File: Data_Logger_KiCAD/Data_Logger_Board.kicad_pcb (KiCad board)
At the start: 4 copper layers, 45 x 64.8 mm, 110 parts, among them J1 USB_C_Receptacle_USB2.0_16P, J2 Screw_Terminal_01x02, J3 Micro_SD_Card, J4 Conn_Coaxial_Small, J5 Conn_01x02, Q1 Q_NMOS_GSD, SW1 SW_Push, SW2 SW_Push, U1 LSM6DSO32TR, U10 BMP390L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

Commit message: fix merge
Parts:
- moved C37 8.78 mm to (158.2, 96.6), turned to 180 degrees
- moved D5 3.10 mm to (162.1, 96.6)
- moved R25 2.10 mm to (121.4, 55.7)
- moved R20 0.90 mm to (156.7, 106.4)
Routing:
- net +3V3: track 166.9 -> 85.8 mm, vias 27 -> 25
- net Net-(U6-VBAT): track 19.4 -> 13.0 mm, vias 3 -> 2
- net Net-(D6-A): track 2.12 -> 0.00 mm
- net /MCU/~{MS_CS}: track 45.4 -> 43.9 mm
- net +BATT: track 2.79 -> 4.22 mm
- net /MCU/PWR_IN: track 23.4 -> 24.5 mm
- net Net-(D2-A): track 2.10 -> 1.20 mm
- net /MCU/MOSI: track 113.3 -> 112.4 mm
- net /MCU/RADIO_INT: track 19.8 -> 19.0 mm
- net /MCU/BATTERY_SENSE: track 23.2 -> 23.9 mm
- net /MCU/ANT_SW: track 48.0 -> 47.5 mm
- net /MCU/~{IMU_CS}: track 29.4 -> 29.5 mm, vias 2 -> 3
- net GND: vias 457 -> 510
- added copper zone on In3.Cu, net +3V3
- added copper zone on In4.Cu, net GND
- removed copper zone on In2.Cu, net +3V3
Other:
- copper layers 4 -> 6

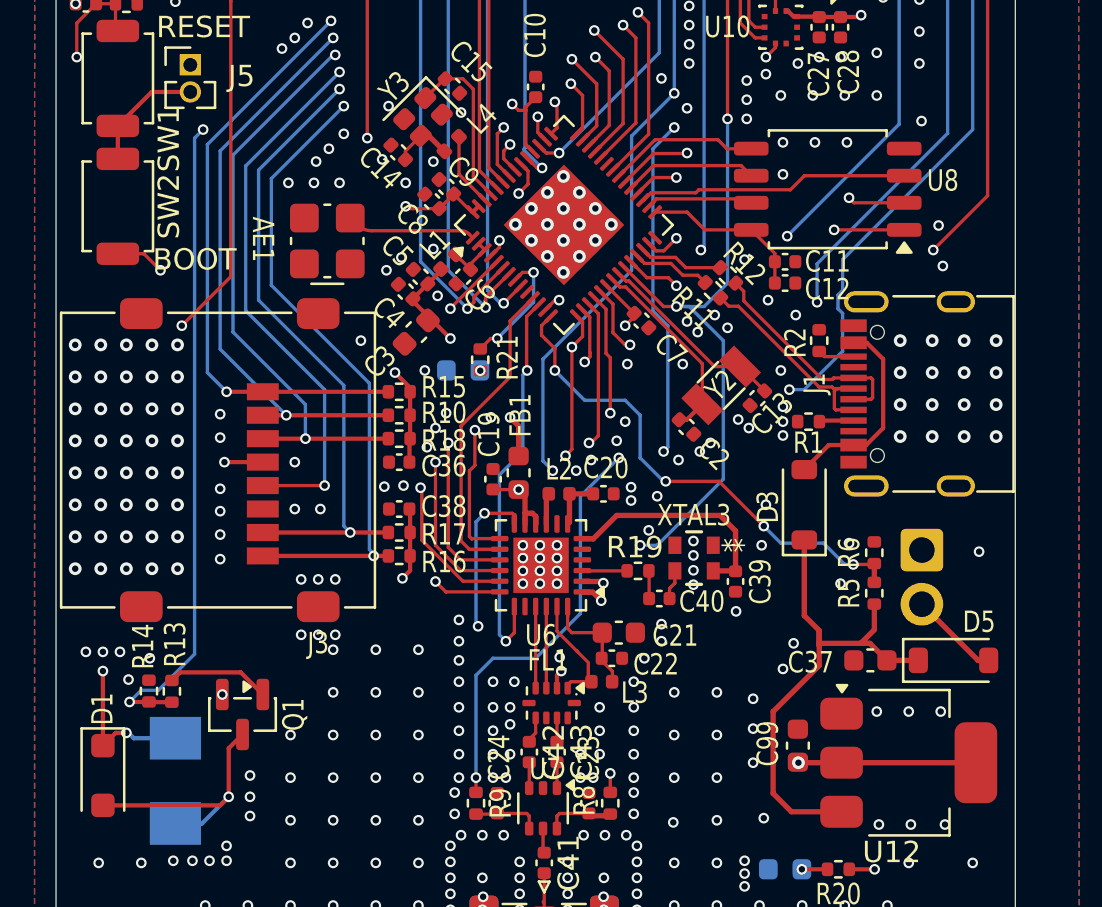
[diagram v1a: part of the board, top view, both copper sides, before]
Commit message: four layer creation
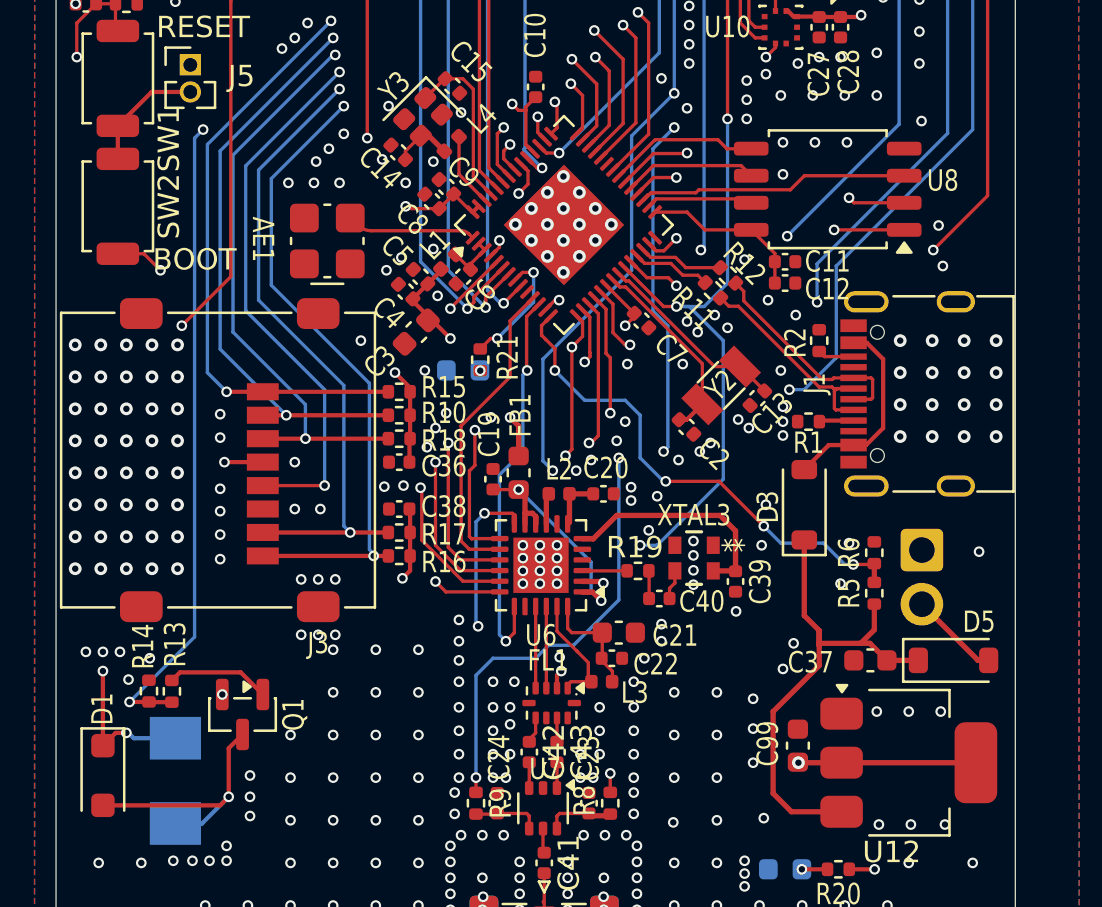
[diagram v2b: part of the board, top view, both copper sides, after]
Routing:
- net Net-(U6-VBAT): track 13.0 -> 12.3 mm
- net /MCU/ANT_SW: track 47.5 -> 48.2 mm
- removed copper zone on In3.Cu, net +3V3
- removed copper zone on In4.Cu, net GND
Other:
- copper layers 6 -> 4
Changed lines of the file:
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@@
 		(4 "In1.Cu" power)
 		(6 "In2.Cu" signal)
-		(8 "In3.Cu" signal)
-		(10 "In4.Cu" power)
 		(2 "B.Cu" signal)
 		(9 "F.Adhes" user "F.Adhesive")
@@
 			(layer "dielectric 1"
 				(type "prepreg")
-				(thickness 0.0994)
+				(thickness 0.1)
 				(material "3313*1")
 				(epsilon_r 4.5)
@@
 			(layer "dielectric 2"
 				(type "core")
-				(thickness 0.55)
+				(thickness 1.238)
 				(material "Core")
 				(epsilon_r 4.5)
@@
 			(layer "dielectric 3"
 				(type "prepreg")
-				(thickness 0.1088)
+				(thickness 0.1)
 				(material "2116*1")
 				(epsilon_r 4.5)
 				(loss_tangent 0.02)
 			)
-			(layer "In3.Cu"
-				(type "copper")
-				(thickness 0.0152)
-			)
-			(layer "dielectric 4"
-				(type "core")
-				(thickness 0.55)
-				(material "Core")
-				(epsilon_r 4.5)
-				(loss_tangent 0.02)
-			)
-			(layer "In4.Cu"
-				(type "copper")
-				(thickness 0.0152)
-			)
-			(layer "dielectric 5"
-				(type "prepreg")
-				(thickness 0.0994)
-				(material "3313*1")
-				(epsilon_r 4.5)
-				(loss_tangent 0.02)
-			)
 			(layer "B.Cu"
 				(type "copper")
@@
 			(net 0)
 			(net_name "")
-			(layers "F.Cu" "B.Cu" "In1.Cu" "In2.Cu" "In3.Cu" "In4.Cu")
+			(layers "F.Cu" "B.Cu" "In1.Cu" "In2.Cu")
 			(hatch edge 0.508)
 			(connect_pads
@@
 			(net 0)
 			(net_name "")
-			(layers "F.Cu" "B.Cu" "In1.Cu" "In2.Cu" "In3.Cu" "In4.Cu")
+			(layers "F.Cu" "B.Cu" "In1.Cu" "In2.Cu")
 			(hatch edge 0.508)
 			(connect_pads
@@
 			(net 0)
 			(net_name "")
-			(layers "B.Cu" "In1.Cu" "F.SilkS" "In2.Cu" "In3.Cu" "In4.Cu")
+			(layers "B.Cu" "In1.Cu" "F.SilkS" "In2.Cu")
 			(hatch edge 0.508)
 			(connect_pads
@@
 	)
 	(segment
-		(start 142.5 96.5)
-		(end 144.6 94.4)
+		(start 140.5 96.5)
+		(end 139.7 97.3)
 		(width 0.1565)
 		(layer "B.Cu")
@@
 	)
 	(segment
-		(start 148 80.2)
-		(end 148.7 80.9)
+		(start 146.4 93.765899)
+		(end 144.275149 95.89075)
 		(width 0.1565)
 		(layer "B.Cu")
@@
 	)
 	(segment
-		(start 140.5 96.5)
-		(end 142.5 96.5)
+		(start 139.7 97.3)
+		(end 139.7 102.1)
+		(width 0.1565)
+		(layer "B.Cu")
+		(net 37)
+	)
+	(segment
+		(start 148 80.2)
+		(end 148.7 80.9)
 		(width 0.1565)
 		(layer "B.Cu")
@@
 	)
 	(segment
+		(start 143.10925 95.89075)
+		(end 142.5 96.5)
+		(width 0.1565)
+		(layer "B.Cu")
+		(net 37)
+	)
+	(segment
 		(start 148 72.6)
 		(end 148 80.2)
@@
 	)
 	(segment
-		(start 144.6 94.4)
-		(end 144.6 88.9)
+		(start 146.4 87.1)
+		(end 146.4 93.765899)
 		(width 0.1565)
 		(layer "B.Cu")
@@
 	)
 	(segment
-		(start 139.7 97.3)
-		(end 140.5 96.5)
+		(start 144.275149 95.89075)
+		(end 143.10925 95.89075)
 		(width 0.1565)
 		(layer "B.Cu")
@@
 	)
 	(segment
-		(start 139.7 102.1)
-		(end 139.7 97.3)
+		(start 142.5 96.5)
+		(end 140.5 96.5)
 		(width 0.1565)
 		(layer "B.Cu")
@@
 	)
 	(segment
-		(start 144.6 88.9)
-		(end 146.4 87.1)
-		(width 0.1565)
-		(layer "B.Cu")
-		(net 37)
-	)
-	(segment
 		(start 148.5 86.8)
 		(end 146.7 86.8)
@@
 	)
 	(segment
-		(start 126.9 71.7)
-		(end 126.5 72.1)
-		(width 0.1565)
-		(layer "B.Cu")
-		(net 40)
-	)
-	(segment
 		(start 126.5 72.1)
-		(end 126.5 96.3)
-		(width 0.1565)
-		(layer "B.Cu")
-		(net 40)
-	)
-	(segment
-		(start 124.8 98)
-		(end 124 98)
+		(end 126.5 95.5)
 		(width 0.1565)
 		(layer "B.Cu")
@@
 	)
 	(segment
-		(start 126.5 96.3)
-		(end 124.8 98)
+		(start 126.5 95.5)
+		(end 123.45 98.55)
 		(width 0.1565)
 		(layer "B.Cu")
@@
 	)
 	(segment
-		(start 124 98)
-		(end 123.45 98.55)
+		(start 126.9 71.7)
+		(end 126.5 72.1)
 		(width 0.1565)
 		(layer "B.Cu")
@@
 	)
 	(segment
-		(start 156.9 77.8)
-		(end 163 71.7)
-		(width 0.1565)
-		(layer "B.Cu")
-		(net 64)
-	)
-	(segment
-		(start 154.4 83.9)
-		(end 155.1 83.9)
-		(width 0.1565)
-		(layer "B.Cu")
-		(net 64)
-	)
-	(segment
-		(start 156.9 80.322026)
-		(end 156.68075 80.102776)
-		(width 0.1565)
-		(layer "B.Cu")
-		(net 64)
-	)
-	(segment
-		(start 156.9 82.1)
-		(end 156.9 80.322026)
-		(width 0.1565)
-		(layer "B.Cu")
-		(net 64)
-	)
-	(segment
-		(start 156.68075 80.102776)
-		(end 156.68075 79.457224)
+		(start 155.1 83.9)
+		(end 156.6 82.4)
 		(width 0.1565)
 		(layer "B.Cu")
@@
 	)
 	(segment
-		(start 156.9 79.237974)
-		(end 156.9 77.8)
+		(start 163 71.7)
+		(end 163 60.225)
 		(width 0.1565)
 		(layer "B.Cu")
@@
 	)
 	(segment
-		(start 155.1 83.9)
-		(end 156.9 82.1)
+		(start 154.4 83.9)
+		(end 155.1 83.9)
 		(width 0.1565)
 		(layer "B.Cu")
@@
 	)
 	(segment
-		(start 163 71.7)
-		(end 163 60.225)
+		(start 163 60.225)
+		(end 162.475 59.7)
 		(width 0.1565)
 		(layer "B.Cu")
@@
 	)
 	(segment
-		(start 156.68075 79.457224)
-		(end 156.9 79.237974)
+		(start 156.6 82.4)
+		(end 156.6 78.1)
 		(width 0.1565)
 		(layer "B.Cu")
@@
 	)
 	(segment
-		(start 163 60.225)
-		(end 162.475 59.7)
+		(start 156.6 78.1)
+		(end 163 71.7)
 		(width 0.1565)
 		(layer "B.Cu")
@@
 	)
 	(segment
-		(start 145.11575 93.34075)
-		(end 145.575 93.8)
+		(start 145.1 93.325)
+		(end 145.1 91.9875)
 		(width 0.1565)
-		(layer "In3.Cu")
-		(net 112)
-	)
-	(segment
-		(start 144.5 90.1)
-		(end 145.11575 90.71575)
-		(width 0.1565)
-		(layer "In3.Cu")
-		(net 112)
-	)
-	(segment
-		(start 141.7 88.5875)
-		(end 143.2125 90.1)
-		(width 0.1565)
-		(layer "In3.Cu")
+		(layer "B.Cu")
 		(net 112)
 	)
 	(segment
-		(start 143.2125 90.1)
-		(end 144.5 90.1)
+		(start 145.1 91.9875)
+		(end 141.7 88.5875)
 		(width 0.1565)
-		(layer "In3.Cu")
+		(layer "B.Cu")
 		(net 112)
 	)
 	(segment
-		(start 145.11575 90.71575)
-		(end 145.11575 93.34075)
+		(start 145.575 93.8)
+		(end 145.1 93.325)
 		(width 0.1565)
-		(layer "In3.Cu")
+		(layer "B.Cu")
 		(net 112)
 	)
@@
 		(net 1)
 		(net_name "GND")
-		(layers "F.Cu" "B.Cu" "In1.Cu" "In2.Cu" "In4.Cu")
+		(layers "F.Cu" "B.Cu" "In1.Cu" "In2.Cu")
 		(hatch edge 0.5)
 		(connect_pads yes
@@
 			)
 		)
-	)
-	(zone
-		(net 5)
-		(net_name "+3V3")
-		(layer "In3.Cu")
-		(hatch edge 0.5)
-		(priority 3)
-		(connect_pads yes
-			(clearance 0.127)
-		)
-		(min_thickness 0.127)
-		(filled_areas_thickness no)
-		(fill yes
-			(thermal_gap 0.5)
-			(thermal_bridge_width 0.5)
-		)
-		(polygon
-			(pts
-				(xy 119 34.5) (xy 167.95 34.4) (xy 168 115.15) (xy 119 115.2)
-			)
-		)

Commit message: start power routing
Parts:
- moved R25 2.10 mm to (121.3, 57.8)
- moved R20 0.90 mm to (157.6, 106.4)
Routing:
- net +3V3: track 85.8 -> 185.9 mm, vias 25 -> 26
- net /MCU/ACCEL_INT: track 52.1 -> 54.3 mm
- net Net-(D6-A): track 0.00 -> 2.12 mm
- net Net-(D2-A): track 1.20 -> 2.10 mm
- net /MCU/~{IMU_CS}: track 29.5 -> 29.4 mm, vias 3 -> 2
- net GND: vias 510 -> 473
- added copper zone on In2.Cu, net +3V3

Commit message: ready for review
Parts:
- moved C37 8.78 mm to (154.8, 104.7), turned to -90 degrees
- moved D5 3.10 mm to (159.0, 96.6)
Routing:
- net +3V3: track 185.9 -> 159.8 mm, vias 26 -> 27
- net Net-(U6-VBAT): track 12.3 -> 19.4 mm, vias 2 -> 3
- net /MCU/ACCEL_INT: track 54.3 -> 52.1 mm
- net +BATT: track 4.22 -> 2.79 mm
- net /MCU/PWR_IN: track 24.7 -> 23.4 mm
- net /MCU/MOSI: track 112.4 -> 113.3 mm
- net /MCU/~{MS_CS}: track 43.9 -> 44.5 mm
- net /MCU/RADIO_INT: track 19.3 -> 19.8 mm
- net GND: vias 473 -> 457

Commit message: fix connections
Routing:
- net +3V3: track 159.8 -> 166.9 mm
- net /MCU/~{MS_CS}: track 44.5 -> 45.4 mm
- net /MCU/BATTERY_SENSE: track 23.9 -> 23.2 mm
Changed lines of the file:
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@@
 	)
 	(segment
+		(start 141.3 85.2)
+		(end 142.272986 85.2)
+		(width 0.25)
+		(layer "In2.Cu")
+		(net 5)
+	)
+	(segment
 		(start 146.15 48.4)
 		(end 145.85 48.1)
@@
 	)
 	(segment
+		(start 146.572986 80.9)
+		(end 146.7 80.9)
+		(width 0.25)
+		(layer "In2.Cu")
+		(net 5)
+	)
+	(segment
 		(start 145.8 60.1)
 		(end 139.857014 60.1)
@@
 	)
 	(segment
+		(start 142.272986 85.2)
+		(end 146.572986 80.9)
+		(width 0.25)
+		(layer "In2.Cu")
+		(net 5)
+	)
+	(segment
 		(start 148.29 48.41)
 		(end 148.28 48.4)
@@
 	)
 	(segment
-		(start 147.4 85.1)
-		(end 146.7 84.4)
+		(start 145.5 84.4)
+		(end 144.8 84.4)
 		(width 0.1565)
 		(layer "B.Cu")
@@
 	)
 	(segment
-		(start 147.4 87.1)
-		(end 147.4 85.1)
+		(start 148.5 88.2)
+		(end 147.4 87.1)
 		(width 0.1565)
 		(layer "B.Cu")
@@
 	)
 	(segment
-		(start 148.5 88.2)
-		(end 147.4 87.1)
+		(start 147.4 87.1)
+		(end 147.4 86.3)
 		(width 0.1565)
 		(layer "B.Cu")
@@
 	)
 	(segment
-		(start 146.7 84.4)
-		(end 144.8 84.4)
+		(start 144.8 84.4)
+		(end 143.4 83)
 		(width 0.1565)
 		(layer "B.Cu")
@@
 	)
 	(segment
-		(start 148.6 88.2)
-		(end 148.5 88.2)
+		(start 147.4 86.3)
+		(end 145.5 84.4)
 		(width 0.1565)
 		(layer "B.Cu")
@@
 	)
 	(segment
-		(start 144.8 84.4)
-		(end 143.4 83)
+		(start 148.6 88.2)
+		(end 148.5 88.2)
 		(width 0.1565)
 		(layer "B.Cu")
@@
 	)
 	(segment
+		(start 154.6 60.95)
+		(end 153.75 60.95)
+		(width 0.1565)
+		(layer "F.Cu")
+		(net 62)
+	)
+	(segment
 		(start 139.6 79.549567)
 		(end 140.961218 78.188349)
@@
 	)
 	(segment
-		(start 145.05 82.175)
-		(end 145.039113 82.164113)
+		(start 144.82 83.51)
+		(end 144.82 82.58)
+		(width 0.1565)
+		(layer "F.Cu")
+		(net 64)
+	)
+	(segment
+		(start 145.039113 80.498478)
+		(end 144.708883 80.168248)
 		(width 0.1565)
 		(layer "F.Cu")
@@
 	)
 	(segment
-		(start 145.05 82.35)
-		(end 145.05 82.175)
+		(start 161.9 59.125)
+		(end 162.475 59.7)
 		(width 0.1565)
 		(layer "F.Cu")
@@
 	)
 	(segment
-		(start 144.8 82.6)
-		(end 145.05 82.35)
+		(start 145.05 82.35)
+		(end 145.05 82.175)
 		(width 0.1565)
 		(layer "F.Cu")
@@
 	)
 	(segment
-		(start 161.9 59.125)
-		(end 162.475 59.7)
+		(start 160.91 59.125)
+		(end 161.9 59.125)
 		(width 0.1565)
 		(layer "F.Cu")
@@
 	)
 	(segment
-		(start 145.039113 80.498478)
-		(end 144.708883 80.168248)
+		(start 145.05 82.175)
+		(end 145.039113 82.164113)
 		(width 0.1565)
 		(layer "F.Cu")
@@
 	)
 	(segment
-		(start 160.91 59.125)
-		(end 161.9 59.125)
+		(start 144.82 82.58)
+		(end 145.05 82.35)
 		(width 0.1565)
 		(layer "F.Cu")
@@
 	)
 	(via
-		(at 144.8 82.6)
+		(at 144.82 83.51)
 		(size 0.5)
 		(drill 0.3)
@@
 	)
 	(segment
-		(start 144.8 82.7)
-		(end 144.8 82.6)
+		(start 154.05925 83.55925)
+		(end 154.4 83.9)
 		(width 0.1565)
 		(layer "In2.Cu")
@@
 	)
 	(segment
-		(start 154.4 83.9)
-		(end 154.1 83.6)
+		(start 153.719101 83.51)
+		(end 153.768351 83.55925)
 		(width 0.1565)
 		(layer "In2.Cu")
@@
 	)
 	(segment
-		(start 145.7 83.6)
-		(end 144.8 82.7)
+		(start 153.768351 83.55925)
+		(end 154.05925 83.55925)
 		(width 0.1565)
 		(layer "In2.Cu")
@@
 	)
 	(segment
-		(start 154.1 83.6)
-		(end 145.7 83.6)
+		(start 144.82 83.51)
+		(end 153.719101 83.51)
 		(width 0.1565)
 		(layer "In2.Cu")
@@
 	)
 	(zone
-		(net 82)
-		(net_name "/MCU/SMA_CONN")
+		(net 107)
+		(net_name "Net-(FL2-OUT)")
 		(layer "F.Cu")
 		(name "$teardrop_padvia$")
 		(hatch none 0.1)
-		(priority 30001)
+		(priority 30003)
 		(attr
 			(teardrop
@@
 		(polygon
 			(pts
-				(xy 142.97415 107.5025) (xy 142.82585 107.5025) (xy 142.338223 108.210723) (xy 142.9 109.7385) (xy 143.461777 108.210723)
+				(xy 134.675 59.17415) (xy 134.675 59.02585) (xy 134.482406 58.941211) (xy 134.299 59.1) (xy 134.482406 59.258789)
 			)
 		)
 	)
 	(zone
-		(net 107)
-		(net_name "Net-(FL2-OUT)")
+		(net 82)
+		(net_name "/MCU/SMA_CONN")
 		(layer "F.Cu")
 		(name "$teardrop_padvia$")
 		(hatch none 0.1)
-		(priority 30003)
+		(priority 30001)
 		(attr
 			(teardrop
@@
 		(polygon
 			(pts
-				(xy 134.675 59.17415) (xy 134.675 59.02585) (xy 134.482406 58.941211) (xy 134.299 59.1) (xy 134.482406 59.258789)
+				(xy 142.97415 107.5025) (xy 142.82585 107.5025) (xy 142.338223 108.210723) (xy 142.9 109.7385) (xy 143.461777 108.210723)
 			)
 		)
@@
 			(pts
 				(xy 165 105) (xy 148.6 105.015556) (xy 148.8 87.7) (xy 138 87.992164) (xy 138 97.6) (xy 137.326203 97.696256)
-				(xy 120 97.6) (xy 120.2 80.7) (xy 149.8 80.993316) (xy 149.8 64.8) (xy 140.3 64.8) (xy 140.4 56)
-				(xy 140.4 57.5) (xy 140.7 57.5) (xy 162.4 57.4) (xy 162.3 55.4) (xy 140.407954 55.300036) (xy 140.5 47.2)
+				(xy 120 97.6) (xy 120.2 80.7) (xy 149.8 80.993316) (xy 149.8 64.8) (xy 140.3 64.8) (xy 140.4 57.88)
+				(xy 140.38 57.5) (xy 140.7 57.5) (xy 162.3 57.4) (xy 162.3 55.4) (xy 140.407954 55.300036) (xy 140.5 47.2)
 				(xy 165.3 46.9)
 			)
